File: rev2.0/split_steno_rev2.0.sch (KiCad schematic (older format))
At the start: 65 parts, among them J1 Audio-Jack-4, J2 USB_OTG, P1 TC2030-IDC, SW1 SW_Push, SW10 SW_Push, SW11 SW_Push, SW12 SW_Push, SW13 SW_Push, SW14 SW_Push, SW15 SW_Push, SW16 SW_Push, SW17 SW_Push, SW18 SW_Push, SW19 SW_Push, SW2 SW_Push, SW20 SW_Push, SW21 SW_Push, SW22 Switch-6P-2S2T, SW3 SW_Push, SW4 SW_Push, SW5 SW_Push, SW6 SW_Push, SW7 SW_Push, SW8 SW_Push, SW9 SW_Push, U1 74LVC1G34, U2 MCP73831, U3 MCP1700, U4 MCP1700, U5 ATXMEGA128A4U-AU, U6 nRF24L01_module

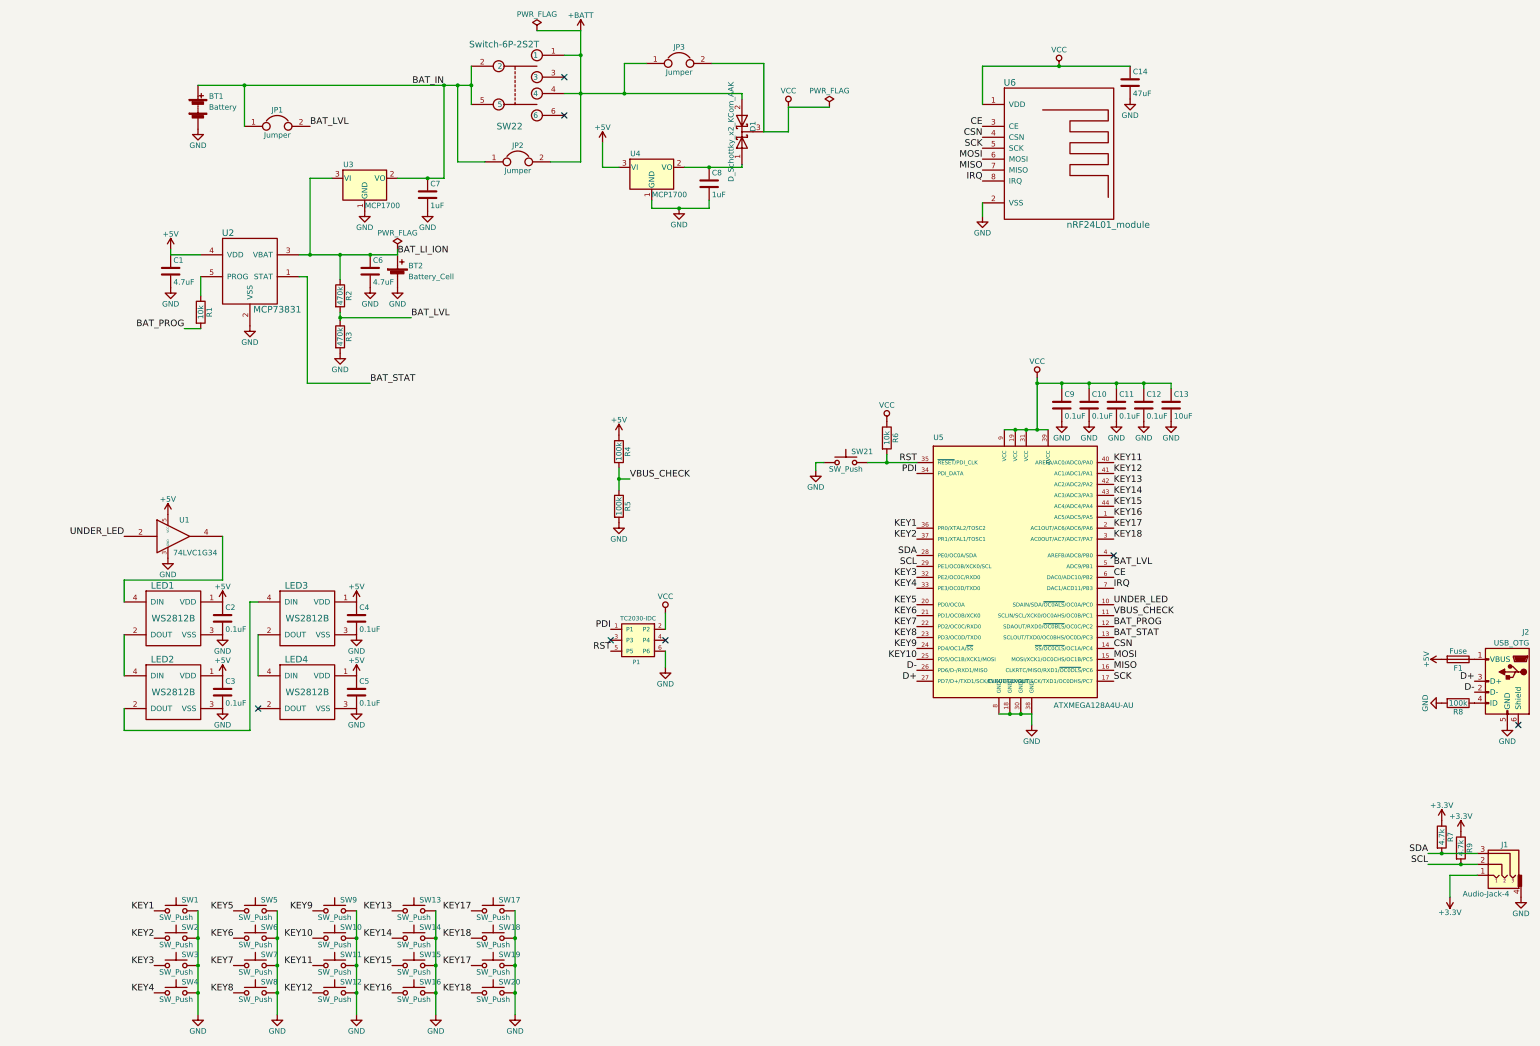
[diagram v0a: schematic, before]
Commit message: reduced components, laid out pcb
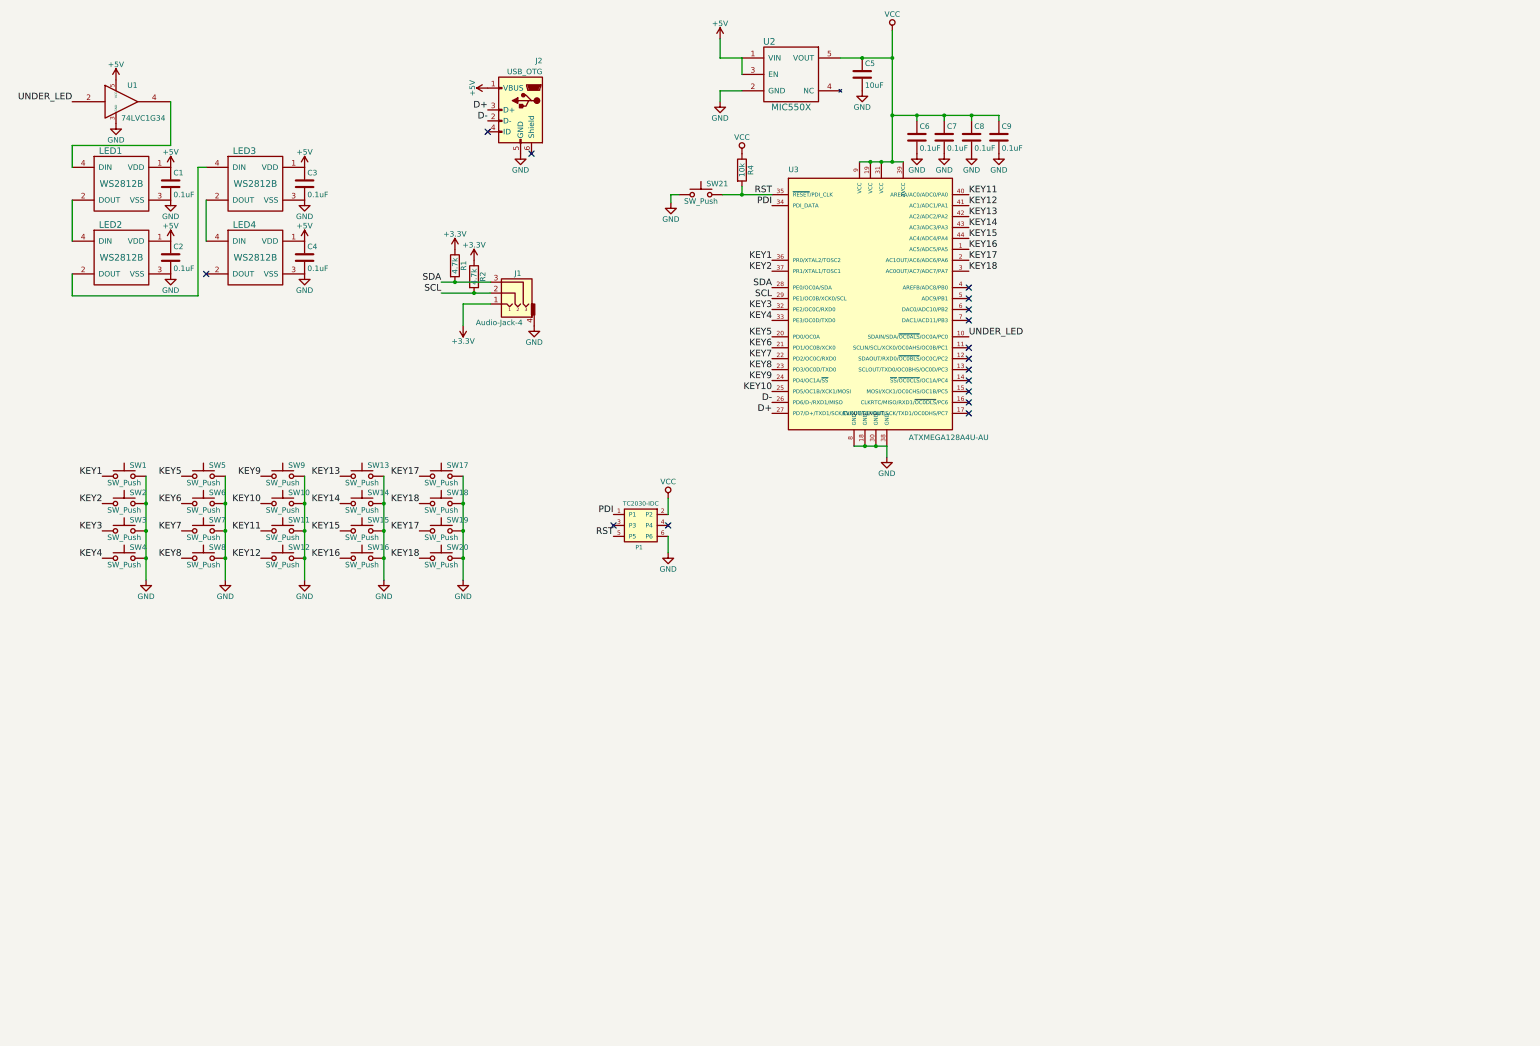
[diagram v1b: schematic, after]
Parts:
- removed BT1: Battery, Battery_Holders:Keystone_1058_1x2032-CoinCell, symbol Battery
- removed BT2: Battery_Cell, Connectors_JST:JST_PH_S2B-PH-K_02x2.00mm_Angled, symbol Battery_Cell
- removed C1, C6: 4.7uF, Capacitors_SMD:C_0603_HandSoldering, symbol C
- removed C13: 10uF, Capacitors_SMD:C_0603_HandSoldering, symbol C
- removed C14: 47uF, Capacitors_SMD:C_0603_HandSoldering, symbol C
- removed C7, C8: 1uF, Capacitors_SMD:C_0603_HandSoldering, symbol C
- removed D1: D_Schottky_x2_KCom_AAK, TO_SOT_Packages_SMD:SOT-23_Handsoldering, symbol D_Schottky_x2_KCom_AAK
- removed F1: Fuse, Fuse_Holders_and_Fuses:Fuse_SMD1206_HandSoldering, symbol Fuse
- removed JP1, JP2, JP3: Jumper, keyboard_parts:SOLDER_JUMPER_2, symbol Jumper
- removed R1: 10k, Resistors_SMD:R_0603_HandSoldering, symbol R
- removed R2, R3: 470k, Resistors_SMD:R_0603_HandSoldering, symbol R
- removed R4, R5, R8: 100k, Resistors_SMD:R_0603_HandSoldering, symbol R
- removed SW22: Switch-6P-2S2T, switch:SlideSwitch_C&K_JS202011CQN, symbol Switch-6P-2S2T
- removed U2: MCP73831, TO_SOT_Packages_SMD:SOT-23-5_HandSoldering, symbol MCP73831
- removed U3, U4: MCP1700, TO_SOT_Packages_SMD:SOT-23, symbol MCP1700
- removed U6: nRF24L01_module, nordic:NRF24L01-Module-SMD, symbol nRF24L01_module
- added C5: 10uF, Capacitors_SMD:C_0603_HandSoldering, symbol C
- added U2: MIC550X, TO_SOT_Packages_SMD:SOT-23-5_HandSoldering, symbol MIC550X
- renumbered C2 to C1, C3 to C2, C4 to C3, C5 to C4, C9 to C6, C10 to C7, C11 to C8, C12 to C9, R7 to R1, R9 to R2, R6 to R4, U5 to U3
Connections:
- net +5V: now also J2.1 (VBUS), U2.1 (VIN), U2.3 (EN)
- net GND: now also C5.2, U2.2 (GND)
- net VCC: now also C5.1, U2.5 (VOUT)
- net BAT_LVL: no longer names the net of U3.5 (ADC9/PB1)
- net BAT_PROG: no longer names the net of U3.12 (SDAOUT/RXD0/~OC0BLS~/OC0C/PC2)
- net BAT_STAT: no longer names the net of U3.13 (SCLOUT/TXD0/OC0BHS/OC0D/PC3)
- net CE: no longer names the net of U3.6 (DAC0/ADC10/PB2)
- net CSN: no longer names the net of U3.14 (~SS~/~OC0CLS~/OC1A/PC4)
- net IRQ: no longer names the net of U3.7 (DAC1/ACD11/PB3)
- net MISO: no longer names the net of U3.16 (CLKRTC/MISO/RXD1/~OC0DLS~/PC6)
- net MOSI: no longer names the net of U3.15 (MOSI/XCK1/OC0CHS/OC1B/PC5)
- net SCK: no longer names the net of U3.17 (EVOUT/CLKOUT/SCK/TXD1/OC0DHS/PC7)
- net VBUS_CHECK: no longer names the net of U3.11 (SCLIN/SCL/XCK0/OC0AHS/OC0B/PC1)
- no-connect marks 7 -> 16
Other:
- moved on the sheet: C1, C2, C3, C4, C6, C7, C8, C9, J1, J2, LED1, LED2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
